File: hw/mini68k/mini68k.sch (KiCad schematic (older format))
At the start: 31 parts, among them J1 Jack-DC, J2 6-bit input port, J3 8-bit output port, J4 FTDI header COM1, J5 FTDI header COM2, SW1 SW_SPDT, SW2 SW_Push, U1 HM62256BLP-7, U2 68008D, U3 L7805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

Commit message: more updated footprints and 3d
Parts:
- C1: footprint Capacitors_THT:CP_Radial_D5.0mm_P2.50mm -> Capacitor_THT:CP_Radial_D5.0mm_P2.50mm
- C2: footprint Capacitors_THT:CP_Radial_D5.0mm_P2.00mm -> Capacitor_THT:CP_Radial_D5.0mm_P2.50mm
- D1: footprint Diodes_THT:D_DO-35_SOD27_P10.16mm_Horizontal -> Diode_THT:D_DO-35_SOD27_P10.16mm_Horizontal
- D2: footprint LEDs:LED_D4.0mm -> LED_THT:LED_D4.0mm
- J1: footprint Connectors:BARREL_JACK -> Connector_BarrelJack:BarrelJack_Horizontal
- J4, J5: footprint Connector_PinHeader_2.54mm:PinHeader_1x06_P2.54mm_Vertical -> Connector_PinHeader_2.54mm:PinHeader_1x06_P2.54mm_Horizontal
- JP1: footprint Pin_Headers:Pin_Header_Straight_1x02_Pitch2.54mm -> Connector_PinHeader_2.54mm:PinHeader_1x02_P2.54mm_Vertical
- R1: footprint Resistors_THT:R_Axial_DIN0207_L6.3mm_D2.5mm_P7.62mm_Horizontal -> Resistor_THT:R_Axial_DIN0207_L6.3mm_D2.5mm_P7.62mm_Horizontal
- RN1: footprint Resistors_THT:R_Array_SIP7 -> Resistor_THT:R_Array_SIP7
- SW2: footprint Buttons_Switches_THT:SW_PUSH_6mm -> Button_Switch_THT:SW_PUSH_6mm
- U3: footprint TO_SOT_Packages_THT:TO-220-3_Horizontal -> Package_TO_SOT_THT:TO-220-3_Horizontal_TabDown
- X1: footprint Oscillators:Oscillator_DIP-14 -> Oscillator:Oscillator_DIP-14_LargePads
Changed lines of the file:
@@
 F 0 "U3" H 2800 5075 50  0000 C CNN
 F 1 "L7805" H 2950 5075 50  0000 L CNN
-F 2 "TO_SOT_Packages_THT:TO-220-3_Horizontal" H 2975 4800 50  0001 L CIN
+F 2 "Package_TO_SOT_THT:TO-220-3_Horizontal_TabDown" H 2975 4800 50  0001 L CIN
 F 3 "" H 2950 4900 50  0001 C CNN
 	1    2950 4950
@@
 F 0 "J1" H 950 5360 50  0000 C CNN
 F 1 "Jack-DC" H 950 4975 50  0000 C CNN
-F 2 "Connectors:BARREL_JACK" H 1000 5110 50  0001 C CNN
+F 2 "Connector_BarrelJack:BarrelJack_Horizontal" H 1000 5110 50  0001 C CNN
 F 3 "" H 1000 5110 50  0001 C CNN
 	1    950  5150
@@
 F 0 "C2" H 3425 5200 50  0000 L CNN
 F 1 "10uF" H 3425 5000 50  0000 L CNN
-F 2 "Capacitors_THT:CP_Radial_D5.0mm_P2.00mm" H 3400 5100 50  0001 C CNN
+F 2 "Capacitor_THT:CP_Radial_D5.0mm_P2.50mm" H 3400 5100 50  0001 C CNN
 F 3 "" H 3400 5100 50  0001 C CNN
 	1    3400 5100
@@
 F 0 "C1" H 2425 5200 50  0000 L CNN
 F 1 "100uF" H 2425 5000 50  0000 L CNN
-F 2 "Capacitors_THT:CP_Radial_D5.0mm_P2.50mm" H 2400 5100 50  0001 C CNN
+F 2 "Capacitor_THT:CP_Radial_D5.0mm_P2.50mm" H 2400 5100 50  0001 C CNN
 F 3 "" H 2400 5100 50  0001 C CNN
 	1    2400 5100
@@
 F 0 "D1" H 1450 5150 50  0000 C CNN
 F 1 "D_ALT" H 1450 4950 50  0000 C CNN
-F 2 "Diodes_THT:D_DO-35_SOD27_P10.16mm_Horizontal" H 1450 5050 50  0001 C CNN
+F 2 "Diode_THT:D_DO-35_SOD27_P10.16mm_Horizontal" H 1450 5050 50  0001 C CNN
 F 3 "" H 1450 5050 50  0001 C CNN
 	1    1450 5050
@@
 F 0 "RN1" V 8250 6050 50  0000 C CNN
 F 1 "R_Network06" V 8950 6050 50  0000 C CNN
-F 2 "Resistors_THT:R_Array_SIP7" V 9025 6050 50  0001 C CNN
+F 2 "Resistor_THT:R_Array_SIP7" V 9025 6050 50  0001 C CNN
 F 3 "" H 8650 6050 50  0001 C CNN
 	1    8650 6050
@@
 F 0 "SW2" H 7650 5450 50  0000 L CNN
 F 1 "SW_Push" H 7600 5290 50  0000 C CNN
-F 2 "Buttons_Switches_THT:SW_PUSH_6mm" H 7600 5550 50  0001 C CNN
+F 2 "Button_Switch_THT:SW_PUSH_6mm" H 7600 5550 50  0001 C CNN
 F 3 "" H 7600 5550 50  0001 C CNN
 	1    7600 5350
@@
 F 0 "X1" H 4150 4200 50  0000 L CNN
 F 1 "TCXO-14" H 4400 3700 50  0000 L CNN
-F 2 "Oscillators:Oscillator_DIP-14" H 4800 3600 50  0001 C CNN
+F 2 "Oscillator:Oscillator_DIP-14_LargePads" H 4800 3600 50  0001 C CNN
 F 3 "" H 4250 3950 50  0001 C CNN
 	1    4350 3950
@@
 F 0 "J4" H 4000 2900 50  0000 C CNN
 F 1 "FTDI header COM1" H 4000 2200 50  0000 C CNN
-F 2 "Connector_PinHeader_2.54mm:PinHeader_1x06_P2.54mm_Vertical" H 4000 2600 50  0001 C CNN
+F 2 "Connector_PinHeader_2.54mm:PinHeader_1x06_P2.54mm_Horizontal" H 4000 2600 50  0001 C CNN
 F 3 "" H 4000 2600 50  0001 C CNN
 	1    4000 2600
@@
 F 0 "JP1" H 4550 2750 50  0000 C CNN
 F 1 "Jumper" H 4550 2520 50  0000 C CNN
-F 2 "Pin_Headers:Pin_Header_Straight_1x02_Pitch2.54mm" H 4550 2600 50  0001 C CNN
+F 2 "Connector_PinHeader_2.54mm:PinHeader_1x02_P2.54mm_Vertical" H 4550 2600 50  0001 C CNN
 F 3 "" H 4550 2600 50  0001 C CNN
 	1    4550 2600
@@
 F 0 "D2" H 6650 6050 50  0000 C CNN
 F 1 "RED" H 6650 5850 50  0000 C CNN
-F 2 "LEDs:LED_D4.0mm" H 6650 5950 50  0001 C CNN
+F 2 "LED_THT:LED_D4.0mm" H 6650 5950 50  0001 C CNN
 F 3 "" H 6650 5950 50  0001 C CNN
 	1    6650 5950
@@
 F 0 "R1" V 7130 5950 50  0000 C CNN
 F 1 "330R" V 7050 5950 50  0000 C CNN
-F 2 "Resistors_THT:R_Axial_DIN0207_L6.3mm_D2.5mm_P7.62mm_Horizontal" V 6980 5950 50  0001 C CNN
+F 2 "Resistor_THT:R_Axial_DIN0207_L6.3mm_D2.5mm_P7.62mm_Horizontal" V 6980 5950 50  0001 C CNN
 F 3 "" H 7050 5950 50  0001 C CNN
 	1    7050 5950
@@
 F 0 "J5" H 5400 2100 50  0000 C CNN
 F 1 "FTDI header COM2" H 5400 1400 50  0000 C CNN
-F 2 "Connector_PinHeader_2.54mm:PinHeader_1x06_P2.54mm_Vertical" H 5400 1800 50  0001 C CNN
+F 2 "Connector_PinHeader_2.54mm:PinHeader_1x06_P2.54mm_Horizontal" H 5400 1800 50  0001 C CNN
 F 3 "" H 5400 1800 50  0001 C CNN
 	1    5400 1800

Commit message: better 3d
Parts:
- J4, J5: footprint Connector_PinHeader_2.54mm:PinHeader_1x06_P2.54mm_Horizontal -> Connector_PinHeader_2.54mm:PinHeader_1x06_P2.54mm_Vertical
- SW1: footprint Buttons_Switches_THT:SW_CuK_JS202011CQN_DPDT_Straight -> Button_Switch_THT:SW_E-Switch_EG1271_DPDT
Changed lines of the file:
@@
 F 0 "SW1" H 1850 5220 50  0000 C CNN
 F 1 "SW_SPDT" H 1850 4850 50  0000 C CNN
-F 2 "Buttons_Switches_THT:SW_CuK_JS202011CQN_DPDT_Straight" H 1850 5050 50  0001 C CNN
+F 2 "Button_Switch_THT:SW_E-Switch_EG1271_DPDT" H 1850 5050 50  0001 C CNN
 F 3 "" H 1850 5050 50  0001 C CNN
 	1    1850 5050
@@
 F 0 "J4" H 4000 2900 50  0000 C CNN
 F 1 "FTDI header COM1" H 4000 2200 50  0000 C CNN
-F 2 "Connector_PinHeader_2.54mm:PinHeader_1x06_P2.54mm_Horizontal" H 4000 2600 50  0001 C CNN
+F 2 "Connector_PinHeader_2.54mm:PinHeader_1x06_P2.54mm_Vertical" H 4000 2600 50  0001 C CNN
 F 3 "" H 4000 2600 50  0001 C CNN
 	1    4000 2600
@@
 F 0 "J5" H 5400 2100 50  0000 C CNN
 F 1 "FTDI header COM2" H 5400 1400 50  0000 C CNN
-F 2 "Connector_PinHeader_2.54mm:PinHeader_1x06_P2.54mm_Horizontal" H 5400 1800 50  0001 C CNN
+F 2 "Connector_PinHeader_2.54mm:PinHeader_1x06_P2.54mm_Vertical" H 5400 1800 50  0001 C CNN
 F 3 "" H 5400 1800 50  0001 C CNN
 	1    5400 1800

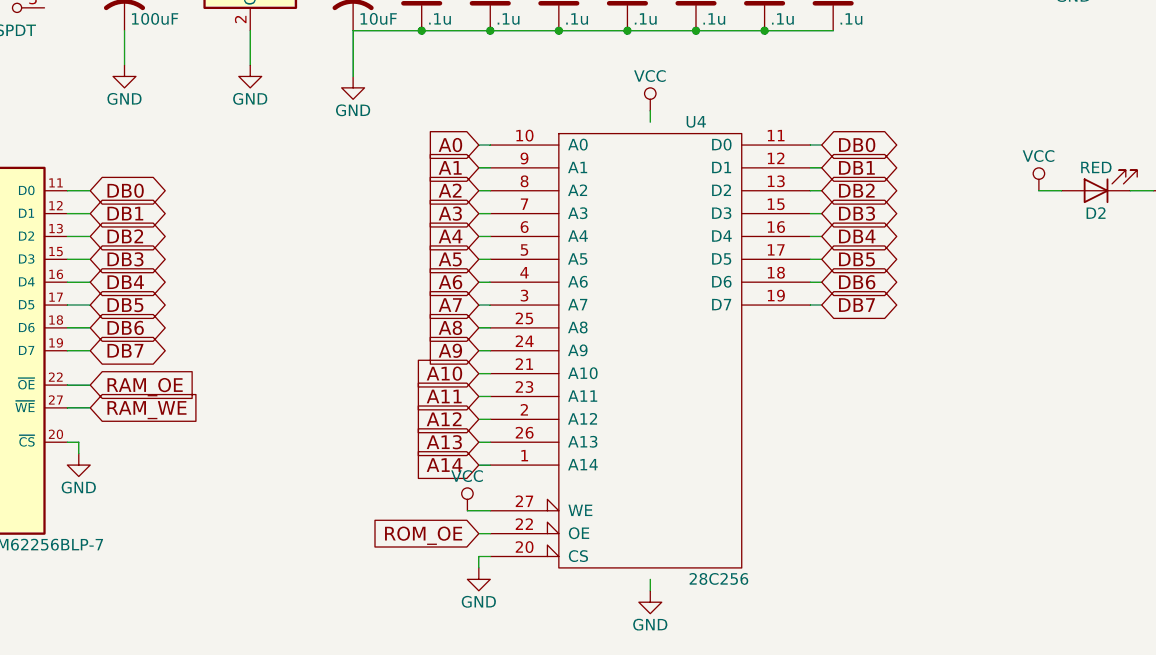
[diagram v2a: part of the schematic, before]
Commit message: jumpers for 27256/28256
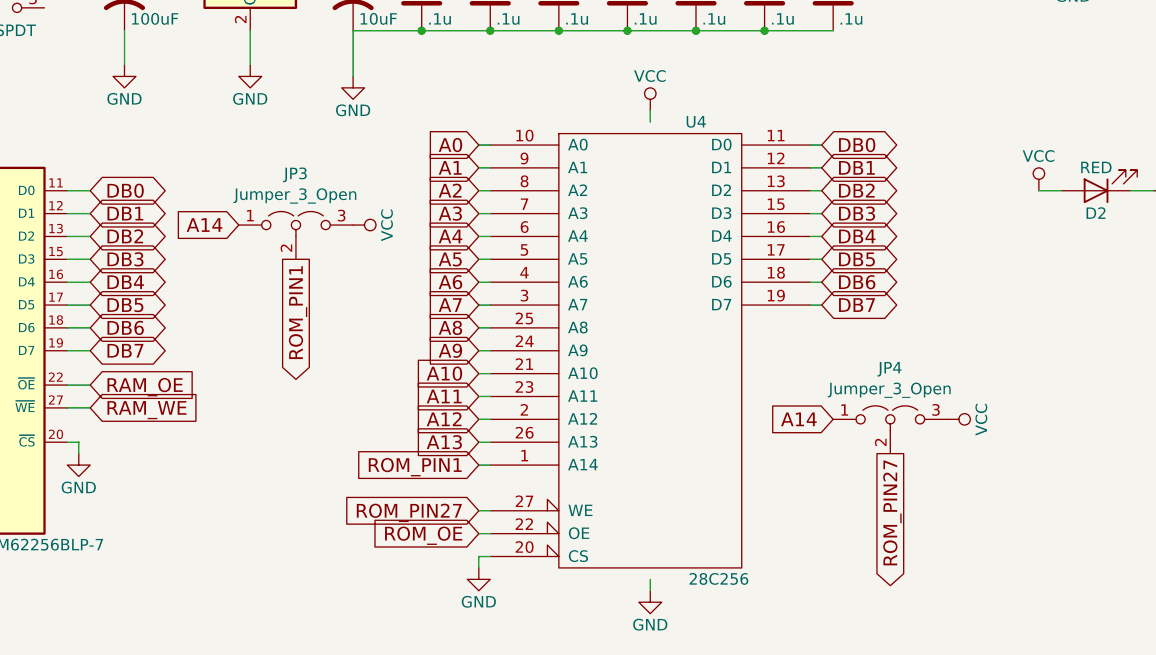
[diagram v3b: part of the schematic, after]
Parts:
- added JP3, JP4: Jumper_3_Open, Connector_PinHeader_2.54mm:PinHeader_1x03_P2.54mm_Vertical, symbol Jumper:Jumper_3_Open
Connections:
- net A14: now also JP3.1 (A), JP4.1 (A); no longer U4.1 (A14)
- net VCC: now also JP3.3 (B), JP4.3 (B); no longer U4.27 (WE)
- new net ROM_PIN1: JP3.2 (C), U4.1 (A14)
- new net ROM_PIN27: JP4.2 (C), U4.27 (WE)
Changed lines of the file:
@@
 Text GLabel 3950 7050 0    60   Input ~ 0
 A13
-Text GLabel 3950 7150 0    60   Input ~ 0
+Text GLabel 2900 6100 0    60   Input ~ 0
 A14
 Text GLabel 1050 5950 0    60   Input ~ 0
@@
 L power:VCC #PWR014
 U 1 1 5B2AD1E7
-P 3900 7350
-F 0 "#PWR014" H 3900 7200 50  0001 C CNN
-F 1 "VCC" H 3900 7500 50  0000 C CNN
-F 2 "" H 3900 7350 50  0001 C CNN
-F 3 "" H 3900 7350 50  0001 C CNN
-	1    3900 7350
-	1    0    0    -1
-$EndComp
-Wire Wire Line
-	4000 7350 3900 7350
+P 6000 6950
+F 0 "#PWR014" H 6000 6800 50  0001 C CNN
+F 1 "VCC" H 6000 7100 50  0000 C CNN
+F 2 "" H 6000 6950 50  0001 C CNN
+F 3 "" H 6000 6950 50  0001 C CNN
+	1    6000 6950
+	0    1    1    0
+$EndComp
 Wire Wire Line
 	6200 3950 6200 3900
@@
 NoConn ~ 5600 1900
 NoConn ~ 5600 1500
+$Comp
+L Jumper:Jumper_3_Open JP4
+U 1 1 5C8940DD
+P 5750 6950
+F 0 "JP4" H 5750 7174 50  0000 C CNN
+F 1 "Jumper_3_Open" H 5750 7083 50  0000 C CNN
+F 2 "Connector_PinHeader_2.54mm:PinHeader_1x03_P2.54mm_Vertical" H 5750 6950 50  0001 C CNN
+F 3 "~" H 5750 6950 50  0001 C CNN
+	1    5750 6950
+	1    0    0    -1
+$EndComp
+$Comp
+L Jumper:Jumper_3_Open JP3
+U 1 1 5C894141
+P 3150 6100
+F 0 "JP3" H 3150 6324 50  0000 C CNN
+F 1 "Jumper_3_Open" H 3150 6233 50  0000 C CNN
+F 2 "Connector_PinHeader_2.54mm:PinHeader_1x03_P2.54mm_Vertical" H 3150 6100 50  0001 C CNN
+F 3 "~" H 3150 6100 50  0001 C CNN
+	1    3150 6100
+	1    0    0    -1
+$EndComp
+Text GLabel 3950 7150 0    60   Input ~ 0
+ROM_PIN1
+Text GLabel 3950 7350 0    60   Input ~ 0
+ROM_PIN27
+Wire Wire Line
+	4000 7350 3950 7350
+Text GLabel 3150 6250 3    60   Output ~ 0
+ROM_PIN1
+Text GLabel 5500 6950 0    60   Input ~ 0
+A14
+Text GLabel 5750 7100 3    60   Output ~ 0
+ROM_PIN27
+$Comp
+L power:VCC #PWR0103
+U 1 1 5C8E58A0
+P 3400 6100
+F 0 "#PWR0103" H 3400 5950 50  0001 C CNN
+F 1 "VCC" H 3400 6250 50  0000 C CNN
+F 2 "" H 3400 6100 50  0001 C CNN
+F 3 "" H 3400 6100 50  0001 C CNN
+	1    3400 6100
+	0    1    1    0
+$EndComp
 $EndSCHEMATC

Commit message: update symbols
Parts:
- J1: symbol mini68k-rescue:Jack-DC -> Connector:Barrel_Jack_Switch
- J4, J5: symbol mini68k-rescue:Conn_01x06_Female -> Connector:Conn_01x06_Male
- SW1: symbol mini68k-rescue:SW_SPDT -> Switch:SW_SPDT
- SW2: symbol mini68k-rescue:SW_Push -> Switch:SW_Push
- U1: symbol mini68k-rescue:HM62256BLP-7 -> Memory_RAM:CY7C199
- U2: symbol mini68k-rescue:68008D -> CPU_NXP_68000:68008D
- U3: symbol mini68k-rescue:L7805 -> Regulator_Linear:L7805
- U4: value 28C256 -> 28C256/27C256; symbol mini68k-rescue:28C256 -> Memory_EEPROM:28C256
- U5: symbol mini68k-rescue:GAL16V8 -> Logic_Programmable:GAL16V8
- U6: symbol mini68k-rescue:MAX708CPA+ -> mini68k:MAX708
- U7: symbol mini68k-rescue:68681 -> Interface:68681
- U8: symbol mini68k-rescue:74LS05 -> 74xx:74LS06
- X1: symbol mini68k-rescue:TCXO-14 -> Oscillator:TCXO-14
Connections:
- wire segments 211 -> 172
- no-connect marks 25 -> 24
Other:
- moved on the sheet: D2, JP1, JP2, JP3, JP4, R1, SW2, X1

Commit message: correct ram pinout... update symbols
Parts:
- added unit 7 of U8
- U1: symbol Memory_RAM:CY7C199 -> Memory_EEPROM:28C256
- U8: symbol 74xx:74LS06 -> 74xx:74LS05
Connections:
- wire segments 172 -> 147
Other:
- moved on the sheet: J4, J5

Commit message: seperate crystal for DUART
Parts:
- added C10: 5pf, Capacitor_THT:C_Disc_D5.0mm_W2.5mm_P2.50mm, symbol Device:C
- added C11: 15pf, Capacitor_THT:C_Disc_D5.0mm_W2.5mm_P2.50mm, symbol Device:C
- added JP5: Jumper, Connector_PinSocket_2.54mm:PinSocket_1x02_P2.54mm_Vertical, symbol Device:Jumper
- added Y1: 3.6864 Mhz, Crystal:Crystal_HC49-4H_Vertical, symbol Device:Crystal
- J3: footprint Connector_PinHeader_2.54mm:PinHeader_1x08_P2.54mm_Vertical -> Connector_PinHeader_2.54mm:PinHeader_1x08_P2.54mm_Horizontal
- J4, J5: footprint Connector_PinHeader_2.54mm:PinHeader_1x06_P2.54mm_Vertical -> Connector_PinHeader_2.54mm:PinHeader_1x06_P2.54mm_Horizontal
- RN1: value R_Network06 -> 1k
- X1: value TCXO-14 -> 8 Mhz
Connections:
- net labels added: X1, X2
- wire segments 147 -> 152
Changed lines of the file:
@@
 EESchema Schematic File Version 4
+LIBS:mini68k-cache
 EELAYER 26 0
 EELAYER END
@@
 Wire Wire Line
 	2400 5250 2400 5400
-Connection ~ 2400 4950
 $Comp
 L Device:D_ALT D1
@@
 P 8650 6050
 F 0 "RN1" V 8250 6050 50  0000 C CNN
-F 1 "R_Network06" V 8950 6050 50  0000 C CNN
+F 1 "1k" V 8950 6050 50  0000 C CNN
 F 2 "Resistor_THT:R_Array_SIP7" V 9025 6050 50  0001 C CNN
 F 3 "" H 8650 6050 50  0001 C CNN
@@
 Wire Wire Line
 	8400 6050 8450 6050
-Text GLabel 7900 1050 0    60   Input ~ 0
+Text GLabel 7450 3800 0    60   Input ~ 0
 CLK
 Wire Wire Line
 	7900 1050 8000 1050
-NoConn ~ 8000 1150
 Text GLabel 7900 2250 0    60   Input ~ 0
 A1
@@
 F 0 "J4" H 3900 2200 50  0000 C CNN
 F 1 "FTDI header COM1" H 3900 1500 50  0000 C CNN
-F 2 "Connector_PinHeader_2.54mm:PinHeader_1x06_P2.54mm_Vertical" H 3900 1900 50  0001 C CNN
+F 2 "Connector_PinHeader_2.54mm:PinHeader_1x06_P2.54mm_Horizontal" H 3900 1900 50  0001 C CNN
 F 3 "" H 3900 1900 50  0001 C CNN
 	1    3900 1900
@@
 Wire Wire Line
 	4900 5250 5200 5250
-Wire Wire Line
-	2400 4950 2650 4950
 Wire Wire Line
 	1400 5250 1400 5400
@@
 F 0 "J3" H 6856 1678 50  0000 C CNN
 F 1 " 8-bit output port" H 6856 1587 50  0000 C CNN
-F 2 "Connector_PinHeader_2.54mm:PinHeader_1x08_P2.54mm_Vertical" H 6750 1200 50  0001 C CNN
+F 2 "Connector_PinHeader_2.54mm:PinHeader_1x08_P2.54mm_Horizontal" H 6750 1200 50  0001 C CNN
 F 3 "~" H 6750 1200 50  0001 C CNN
 	1    6750 1200
@@
 F 0 "J5" H 5350 1300 50  0000 C CNN
 F 1 "FTDI header COM2" H 5350 600 50  0000 C CNN
-F 2 "Connector_PinHeader_2.54mm:PinHeader_1x06_P2.54mm_Vertical" H 5350 1000 50  0001 C CNN
+F 2 "Connector_PinHeader_2.54mm:PinHeader_1x06_P2.54mm_Horizontal" H 5350 1000 50  0001 C CNN
 F 3 "" H 5350 1000 50  0001 C CNN
 	1    5350 1000
@@
 P 4300 3750
 F 0 "X1" H 4100 4000 50  0000 L CNN
-F 1 "TCXO-14" H 4350 3500 50  0000 L CNN
+F 1 "8 Mhz" H 4350 3500 50  0000 L CNN
 F 2 "Oscillator:Oscillator_DIP-14_LargePads" H 4750 3400 50  0001 C CNN
 F 3 "" H 4200 3750 50  0001 C CNN
@@
 	0    -1   -1   0
 $EndComp
+NoConn ~ 2050 5150
+Wire Wire Line
+	2650 4950 2400 4950
+Connection ~ 2400 4950
+$Comp
+L Device:Crystal Y1
+U 1 1 5C8F1BBA
+P 5400 4000
+F 0 "Y1" H 5400 4268 50  0000 C CNN
+F 1 "3.6864 Mhz" H 5400 4150 50  0000 C CNN
+F 2 "Crystal:Crystal_HC49-4H_Vertical" H 5400 4000 50  0001 C CNN
+F 3 "~" H 5400 4000 50  0001 C CNN
+	1    5400 4000
+	1    0    0    -1
+$EndComp
+$Comp
+L Device:Jumper JP5
+U 1 1 5C8F1DCA
+P 7750 3800
+F 0 "JP5" H 7750 4000 50  0000 C CNN
+F 1 "Jumper" H 7750 3700 50  0000 C CNN
+F 2 "Connector_PinSocket_2.54mm:PinSocket_1x02_P2.54mm_Vertical" H 7750 3800 50  0001 C CNN
+F 3 "~" H 7750 3800 50  0001 C CNN
+	1    7750 3800
+	1    0    0    -1
+$EndComp
+Wire Wire Line
+	8000 1150 7900 1150
+Text GLabel 7900 1050 0    60   Input ~ 0
+X1
+Text GLabel 7900 1150 0    60   Input ~ 0
+X2
+Text GLabel 5200 4000 0    60   Output ~ 0
+X1
+Text GLabel 5600 4000 2    60   Output ~ 0
+X2
+Text GLabel 8050 3800 2    60   Output ~ 0
+X1
+$Comp
+L Device:C C11
+U 1 1 5C902842
+P 5550 4150
+F 0 "C11" H 5575 4250 50  0000 L CNN
+F 1 "15pf" H 5575 4050 50  0000 L CNN
+F 2 "Capacitor_THT:C_Disc_D5.0mm_W2.5mm_P2.50mm" H 5588 4000 50  0001 C CNN
+F 3 "" H 5550 4150 50  0001 C CNN
+	1    5550 4150
+	1    0    0    -1
+$EndComp
+$Comp
+L Device:C C10
+U 1 1 5C9028C3
+P 5250 4150
+F 0 "C10" H 5275 4250 50  0000 L CNN
+F 1 "5pf" H 5275 4050 50  0000 L CNN
+F 2 "Capacitor_THT:C_Disc_D5.0mm_W2.5mm_P2.50mm" H 5288 4000 50  0001 C CNN
+F 3 "" H 5250 4150 50  0001 C CNN
+	1    5250 4150
+	1    0    0    -1
+$EndComp
+Wire Wire Line
+	5200 4000 5250 4000
+Connection ~ 5250 4000
+Wire Wire Line
+	5550 4000 5600 4000
+Connection ~ 5550 4000
+Wire Wire Line
+	5250 4300 5400 4300
+$Comp
+L power:GND #PWR0106
+U 1 1 5C92C213
+P 5400 4300
+F 0 "#PWR0106" H 5400 4050 50  0001 C CNN
+F 1 "GND" H 5400 4150 50  0000 C CNN
+F 2 "" H 5400 4300 50  0001 C CNN
+F 3 "" H 5400 4300 50  0001 C CNN
+	1    5400 4300
+	1    0    0    -1
+$EndComp
+Connection ~ 5400 4300
+Wire Wire Line
+	5400 4300 5550 4300
 $EndSCHEMATC

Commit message: backup
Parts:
- removed C9: .1u, Capacitor_THT:C_Disc_D5.0mm_W2.5mm_P2.50mm, symbol Device:C
- removed U8: 74LS05, Package_DIP:DIP-14_W7.62mm_LongPads, symbol 74xx:74LS05
- added J6: Conn_01x20, Connector_PinHeader_2.54mm:PinHeader_1x20_P2.54mm_Horizontal, symbol Connector_Generic:Conn_01x20
- added J7: Conn_01x08, Connector_PinHeader_2.54mm:PinHeader_1x08_P2.54mm_Horizontal, symbol Connector_Generic:Conn_01x08
- added J?: Conn_01x16, symbol Connector_Generic:Conn_01x16
- J2: footprint Connector_PinHeader_2.54mm:PinHeader_1x06_P2.54mm_Vertical -> Connector_PinHeader_2.54mm:PinHeader_1x06_P2.54mm_Horizontal
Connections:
- net labels added: A17, A18, A19
- no-connect marks 24 -> 11
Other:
- moved on the sheet: D2, R1, RN1, SW2, U6
